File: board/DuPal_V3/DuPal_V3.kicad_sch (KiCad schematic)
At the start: 63 parts, among them J1 ZIF Socket, K1 G6K-2, Q1 2N3904, U1 Pico, U10 74HCT166, U11 74HCT166, U12 74HCT166, U13 SN74LV1T125DBV, U2 74HCT595, U3 74HCT595, U4 74HCT595, U5 74HCT595, U6 74HCT595, U7 74HCT02, U8 74HCT166, U9 74HCT166

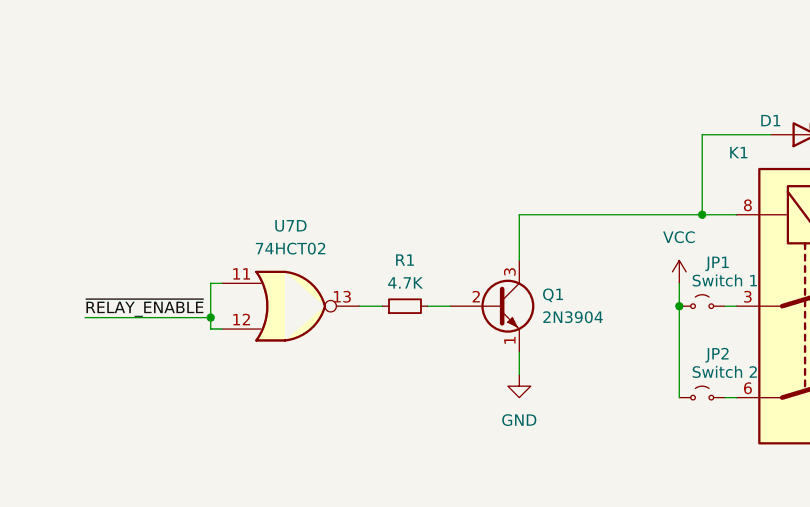
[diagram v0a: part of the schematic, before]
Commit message: Change resistor value
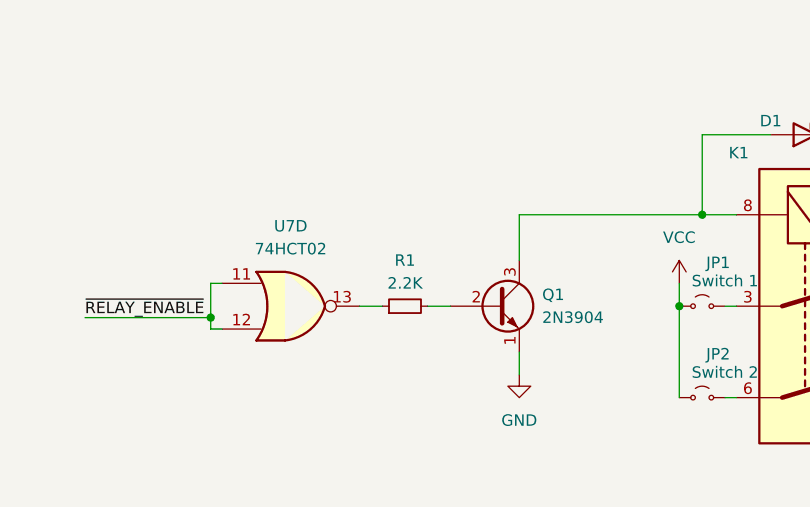
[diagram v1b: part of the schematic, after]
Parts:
- R1: value 4.7K -> 2.2K
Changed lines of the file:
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@@
 			)
 		)
-		(property "Value" "4.7K"
+		(property "Value" "2.2K"
 			(at 91.44 261.62 90)
 			(effects

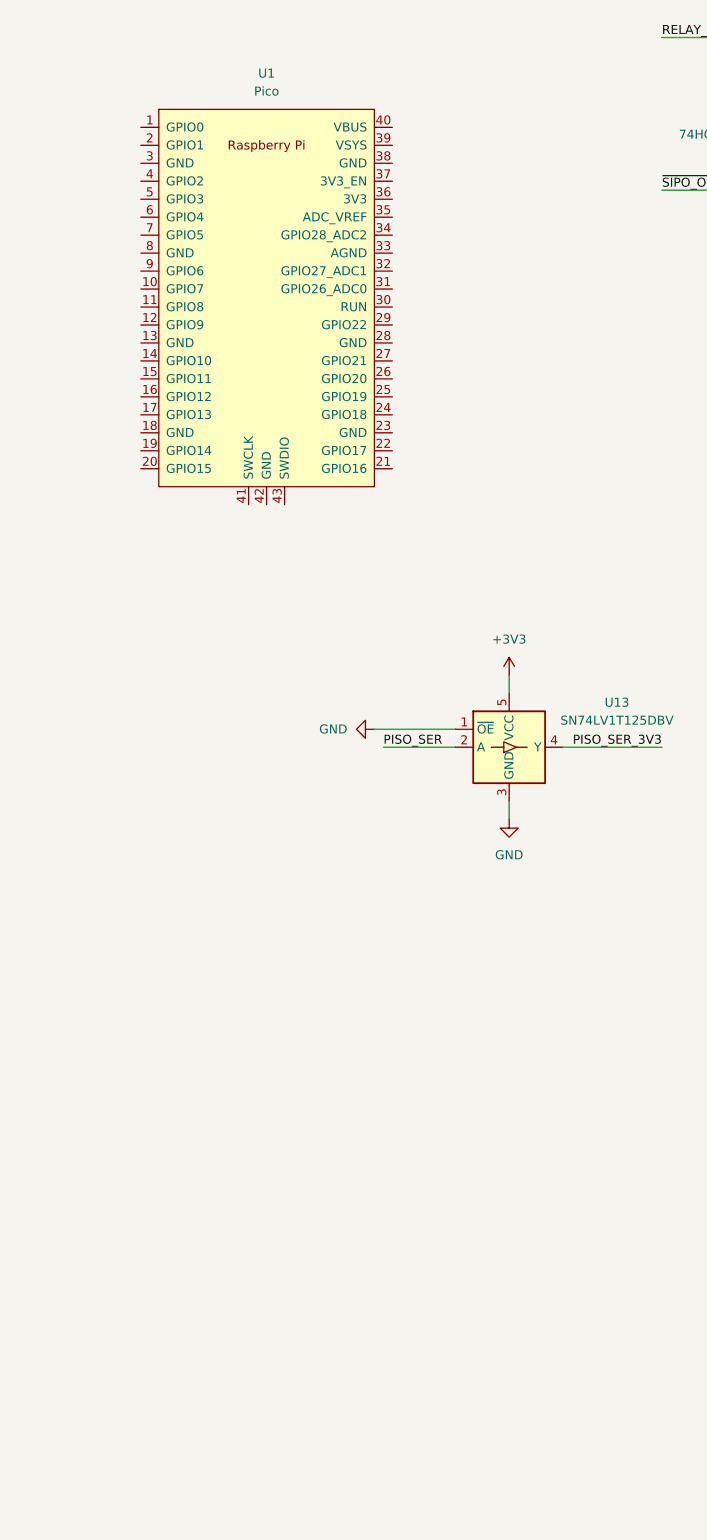
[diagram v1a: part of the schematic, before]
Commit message: Add connections to pico
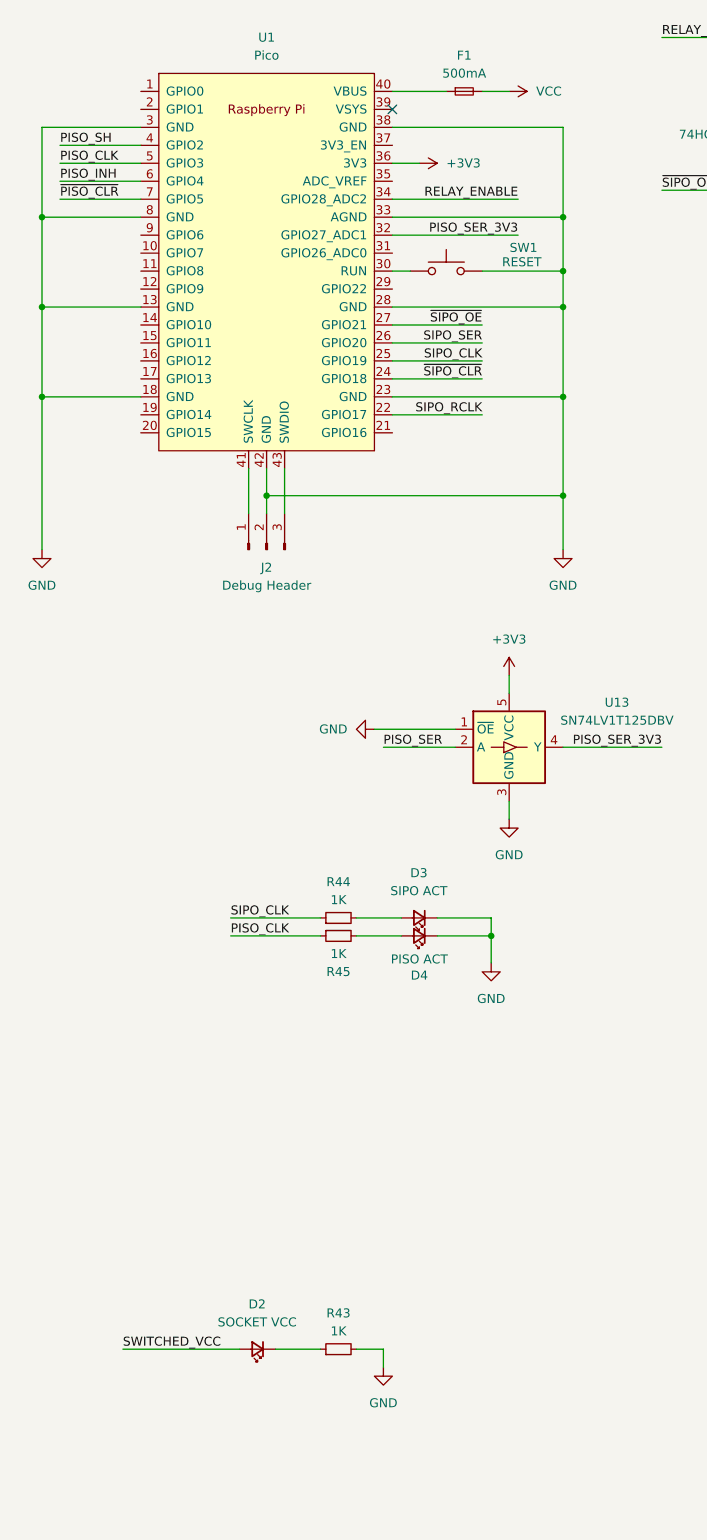
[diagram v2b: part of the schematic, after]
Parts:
- added D2: SOCKET VCC, symbol Device:LED_Small
- added D3: SIPO ACT, symbol Device:LED_Small
- added D4: PISO ACT, symbol Device:LED_Small
- added F1: 500mA, symbol Device:Fuse_Small
- added J2: Debug Header, symbol Connector:Conn_01x03_Pin
- added R43, R44, R45: 1K, symbol Device:R_Small
- added SW1: RESET, symbol Switch:SW_Push
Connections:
- net +3V3: now also U1.36 (3V3)
- net GND: now also U1.13 (GND), U1.18 (GND), U1.23 (GND), U1.28 (GND), U1.3 (GND), U1.33 (AGND), U1.38 (GND), U1.42 (GND), U1.8 (GND), D3.1 (K), D4.1 (K), J2.2 (Pin_2), R43.2, SW1.2
- net PISO_CLK: now also U1.5 (GPIO3), R45.1
- net PISO_INH: now also U1.6 (GPIO4)
- net PISO_SER_3V3: now also U1.32 (GPIO27_ADC1)
- net PISO_SH: now also U1.4 (GPIO2)
- net RELAY_ENABLE: now also U1.34 (GPIO28_ADC2)
- net SIPO_CLK: now also U1.25 (GPIO19), R44.1
- net SIPO_RCLK: now also U1.22 (GPIO17)
- net SIPO_SER: now also U1.26 (GPIO20)
- net SWITCHED_VCC: now also D2.2 (A)
- net VCC: now also F1.2
- net ~{PISO_CLR}: now also U1.7 (GPIO5)
- net ~{SIPO_CLR}: now also U1.24 (GPIO18)
- net ~{SIPO_OE}: now also U1.27 (GPIO21)
- net at U1.30 (RUN): now also SW1.1
- net at U1.40 (VBUS): now also F1.1
- net at U1.41 (SWCLK): now also J2.1 (Pin_1)
- net at U1.43 (SWDIO): now also J2.3 (Pin_3)
- new net: D4.2 (A), R45.2
- new net: D3.2 (A), R44.2
- new net: D2.1 (K), R43.1
- no-connect marks 3 -> 4
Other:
- moved on the sheet: U1

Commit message: Add pulldown resistors for socket
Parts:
- added R46, R47, R48, R49, R50, R51, R52, R53, R54, R55, R56, R57, R58, R59, R60, R61, R62, R63, R64, R65, R66, R67, R68, R69, R70, R71, R72, R73, R74, R75, R76, R77, R78, R79, R80, R81, R82, R83, R84, R85: 100K, symbol Device:R_Small
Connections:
- net GND: now also R46.2, R47.2, R48.2, R49.2, R50.2, R51.2, R52.2, R53.2, R54.2, R55.2, R56.2, R57.2, R58.2, R59.2, R60.2, R61.2, R62.2, R63.2, R64.2, R65.2, R66.2, R67.2, R68.2, R69.2, R70.2, R71.2, R72.2, R73.2, R74.2, R75.2, R76.2, R77.2, R78.2, R79.2, R80.2, R81.2, R82.2, R83.2, R84.2, R85.2
- net SWITCHED_VCC: now also U7.2, U7.3
- net ZIF_1: now also R46.1
- net ZIF_10: now also R55.1
- net ZIF_11: now also R56.1
- net ZIF_12: now also R57.1
- net ZIF_13: now also R58.1
- net ZIF_14: now also R59.1
- net ZIF_15: now also R60.1
- net ZIF_16: now also R61.1
- net ZIF_17: now also R62.1
- net ZIF_18: now also R63.1
- net ZIF_19: now also R64.1
- net ZIF_2: now also R47.1
- net ZIF_20: now also R65.1
- net ZIF_22: now also R66.1
- net ZIF_23: now also R67.1
- net ZIF_24: now also R68.1
- net ZIF_25: now also R69.1
- net ZIF_26: now also R70.1
- net ZIF_27: now also R71.1
- net ZIF_28: now also R72.1
- net ZIF_29: now also R73.1
- net ZIF_3: now also R48.1
- net ZIF_30: now also R74.1
- net ZIF_31: now also R75.1
- net ZIF_32: now also R76.1
- net ZIF_33: now also R77.1
- net ZIF_34: now also R78.1
- net ZIF_35: now also R79.1
- net ZIF_36: now also R80.1
- net ZIF_37: now also R81.1
- net ZIF_38: now also R82.1
- net ZIF_39: now also R83.1
- net ZIF_4: now also R49.1
- net ZIF_40: now also R84.1
- net ZIF_41: now also R85.1
- net ZIF_5: now also R50.1
- net ZIF_6: now also R51.1
- net ZIF_7: now also R52.1
- net ZIF_8: now also R53.1
- net ZIF_9: now also R54.1
- net ~{RELAY_ENABLE}: now also U1.34 (GPIO28_ADC2); no longer U7.1, U7.5
- removed net RELAY_ENABLE: U1.34 (GPIO28_ADC2), U7.2, U7.3
- new net: U7.1, U7.5
- no-connect marks 4 -> 20
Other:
- moved on the sheet: C1, C2, R42

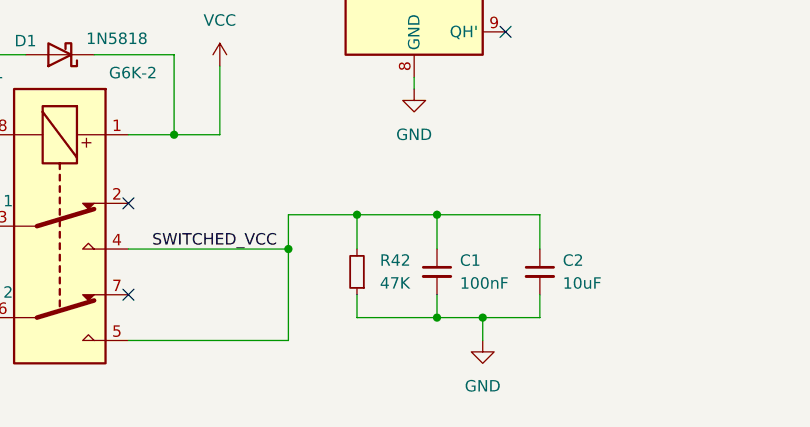
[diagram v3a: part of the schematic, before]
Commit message: Change pulldown res on switched VCC value
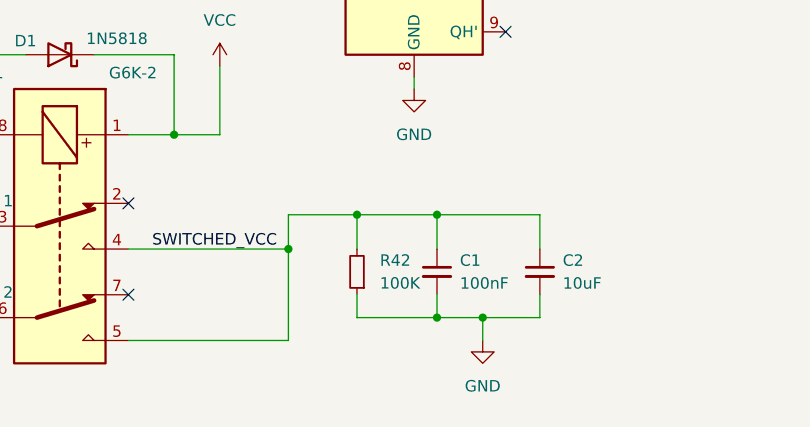
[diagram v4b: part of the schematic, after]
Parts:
- R42: value 47K -> 100K
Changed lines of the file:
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@@
 			)
 		)
-		(property "Value" "47K"
+		(property "Value" "100K"
 			(at 171.45 270.5099 0)
 			(effects

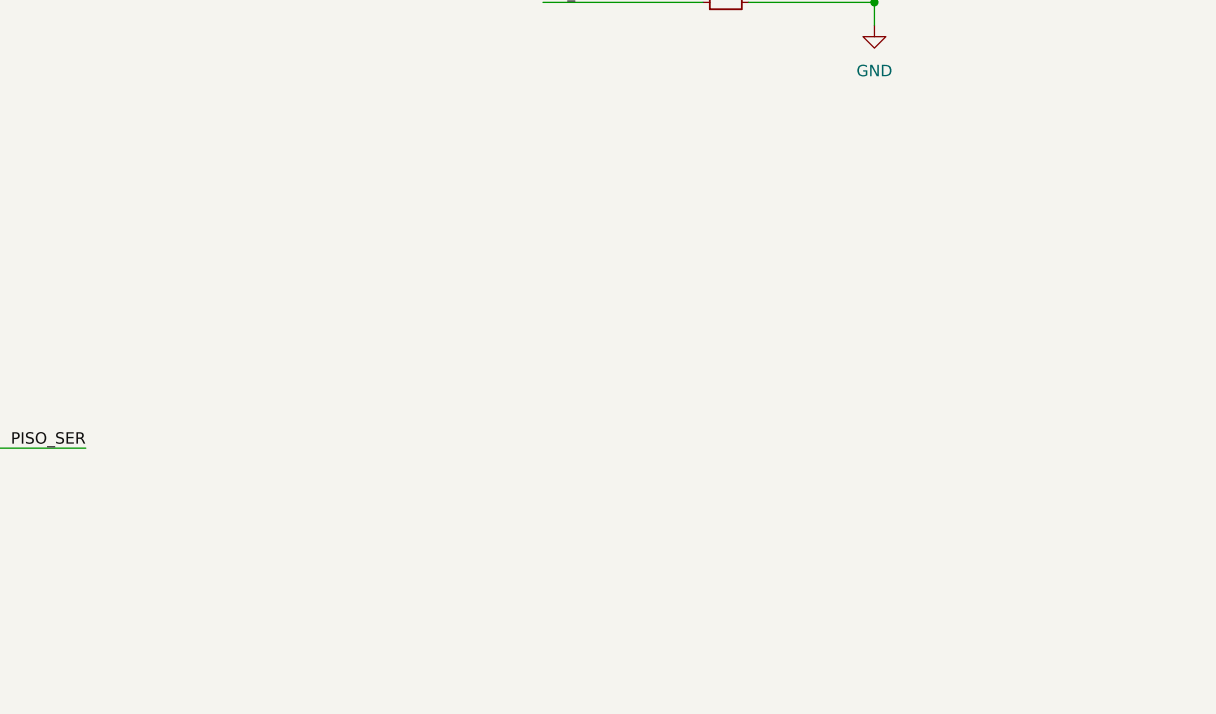
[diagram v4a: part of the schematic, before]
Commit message: Assigned footprints
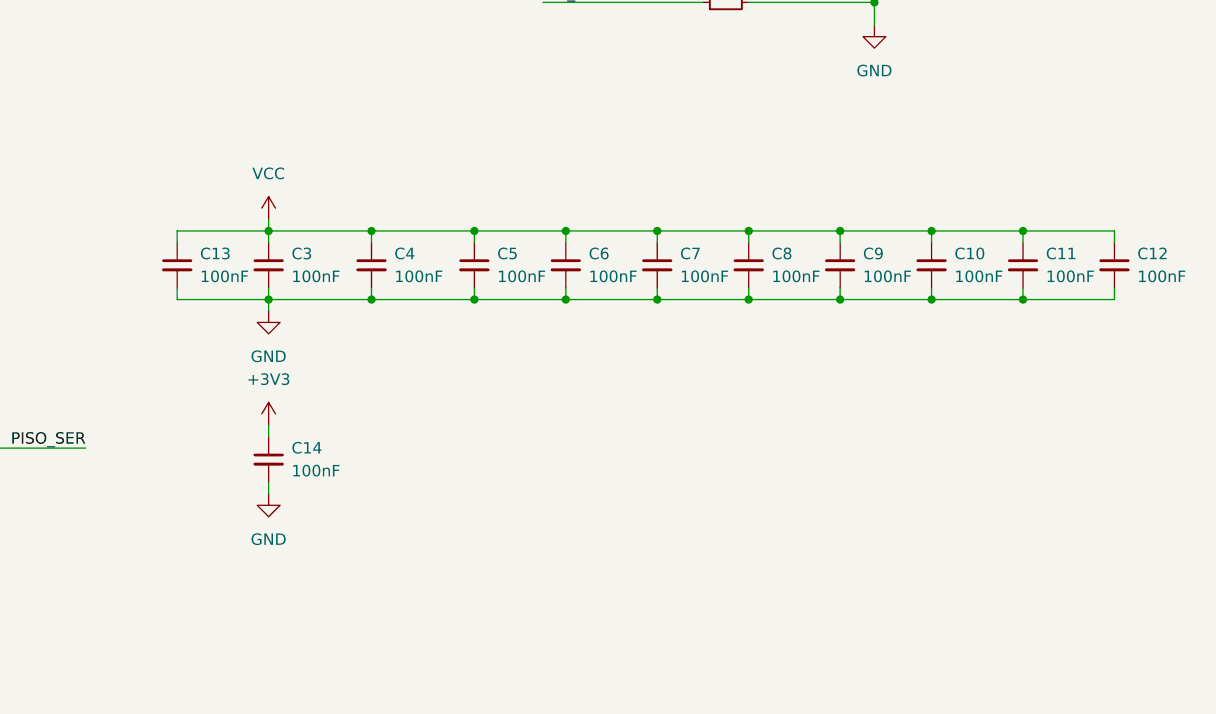
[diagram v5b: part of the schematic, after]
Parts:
- added C10, C11, C12, C13, C14, C3, C4, C5, C6, C7, C8, C9: 100nF, Capacitor_SMD:C_1206_3216Metric_Pad1.33x1.80mm_HandSolder, symbol Device:C_Small
- C1, C2: footprint (none) -> Capacitor_SMD:C_1206_3216Metric_Pad1.33x1.80mm_HandSolder
- D2, D3, D4: footprint (none) -> LED_SMD:LED_1206_3216Metric_Pad1.42x1.75mm_HandSolder
- F1: footprint (none) -> Fuse:Fuse_1206_3216Metric_Pad1.42x1.75mm_HandSolder
- J2: footprint (none) -> Connector_PinHeader_2.54mm:PinHeader_1x03_P2.54mm_Vertical
- JP1, JP2: footprint (none) -> Jumper:SolderJumper-2_P1.3mm_Open_RoundedPad1.0x1.5mm
- K1: footprint (none) -> Relay_THT:Relay_DPDT_Omron_G6K-2P-Y
- R1, R10, R11, R12, R13, R14, R15, R16, R17, R18, R19, R2, R20, R21, R22, R23, R24, R25, R26, R27, R28, R29, R3, R30, R31, R32, R33, R34, R35, R36, R37, R38, R39, R4, R40, R41, R42, R43, R44, R45, R46, R47, R48, R49, R5, R50, R51, R52, R53, R54, R55, R56, R57, R58, R59, R6, R60, R61, R62, R63, R64, R65, R66, R67, R68, R69, R7, R70, R71, R72, R73, R74, R75, R76, R77, R78, R79, R8, R80, R81, R82, R83, R84, R85, R9: footprint (none) -> Resistor_SMD:R_1206_3216Metric_Pad1.30x1.75mm_HandSolder
- SW1: footprint (none) -> Button_Switch_THT:SW_PUSH_6mm
- U10, U11, U12, U2, U3, U4, U5, U6, U8, U9: footprint (none) -> Package_SO:SOIC-16_3.9x9.9mm_P1.27mm
- U7: footprint (none) -> Package_SO:SOIC-14_3.9x8.7mm_P1.27mm
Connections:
- net +3V3: now also C14.1
- net GND: now also C10.2, C11.2, C12.2, C13.2, C14.2, C3.2, C4.2, C5.2, C6.2, C7.2, C8.2, C9.2
- net VCC: now also C10.1, C11.1, C12.1, C13.1, C3.1, C4.1, C5.1, C6.1, C7.1, C8.1, C9.1

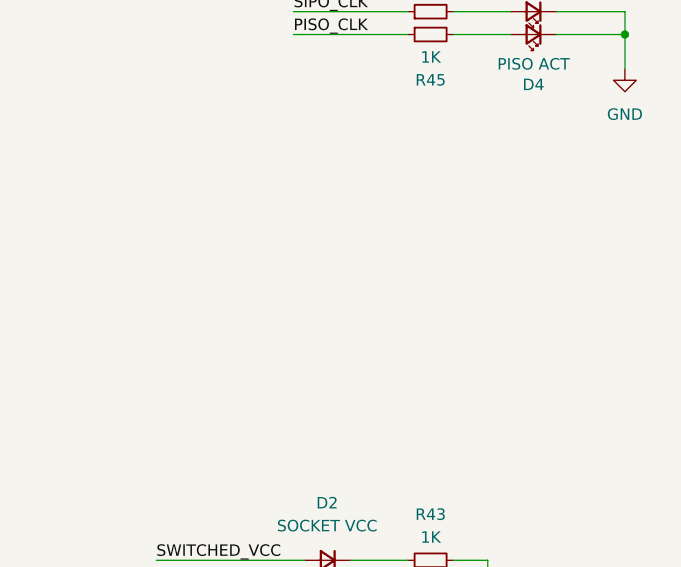
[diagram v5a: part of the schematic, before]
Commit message: Added mounting holes
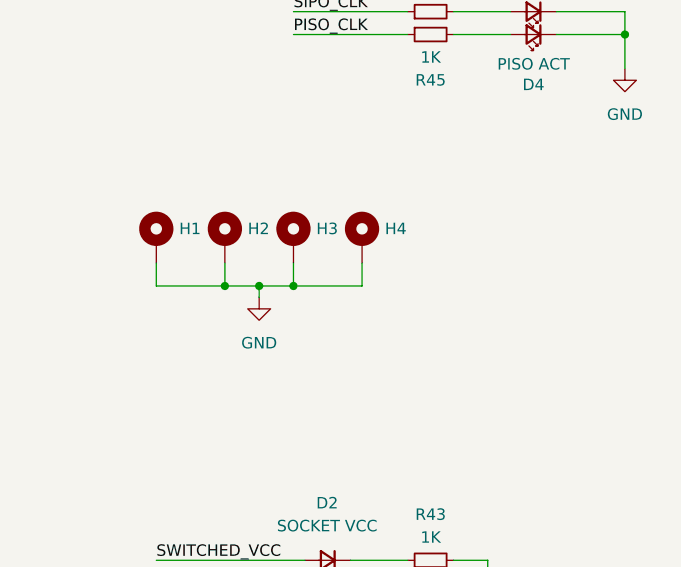
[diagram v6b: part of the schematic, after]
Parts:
- added H1, H2, H3, H4: MountingHole_Pad, MountingHole:MountingHole_3.2mm_M3_DIN965_Pad, symbol Mechanical:MountingHole_Pad
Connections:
- net GND: now also H1.1, H2.1, H3.1, H4.1

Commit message: Cleanup
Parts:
- R43: value 1K -> 1.2K
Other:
- moved on the sheet: C1, C2, D1, D2, JP1, JP2, K1, Q1, R1, R42, R43, U7D

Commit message: Update board
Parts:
- R46, R47, R48, R49, R50, R51, R52, R53, R54, R55, R56, R57, R58, R59, R60, R61, R62, R63, R64, R65, R66, R67, R68, R69, R70, R71, R72, R73, R74, R75, R76, R77, R78, R79, R80, R81, R82, R83, R84, R85: value 100K -> 470K
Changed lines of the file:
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@@
 			)
 		)
-		(property "Value" "100K"
+		(property "Value" "470K"
 			(at 353.822 179.324 90)
 			(effects
@@
 			)
 		)
-		(property "Value" "100K"
+		(property "Value" "470K"
 			(at 353.822 151.384 90)
 			(effects
@@
 			)
 		)
-		(property "Value" "100K"
+		(property "Value" "470K"
 			(at 353.822 176.784 90)
 			(effects
@@
 			)
 		)
-		(property "Value" "100K"
+		(property "Value" "470K"
 			(at 353.822 184.404 90)
 			(effects
@@
 			)
 		)
-		(property "Value" "100K"
+		(property "Value" "470K"
 			(at 353.822 115.824 90)
 			(effects
@@
 			)
 		)
-		(property "Value" "100K"
+		(property "Value" "470K"
 			(at 353.822 105.664 90)
 			(effects
@@
 			)
 		)
-		(property "Value" "100K"
+		(property "Value" "470K"
 			(at 353.822 128.524 90)
 			(effects
@@
 			)
 		)
-		(property "Value" "100K"
+		(property "Value" "470K"
 			(at 353.822 169.164 90)
 			(effects
@@
 			)
 		)
-		(property "Value" "100K"
+		(property "Value" "470K"
 			(at 353.822 103.124 90)
 			(effects
@@
 			)
 		)
-		(property "Value" "100K"
+		(property "Value" "470K"
 			(at 353.822 136.144 90)
 			(effects
@@
 			)
 		)
-		(property "Value" "100K"
+		(property "Value" "470K"
 			(at 353.822 189.484 90)
 			(effects
@@
 			)
 		)
-		(property "Value" "100K"
+		(property "Value" "470K"
 			(at 353.822 148.844 90)
 			(effects
@@
 			)
 		)
-		(property "Value" "100K"
+		(property "Value" "470K"
 			(at 353.822 141.224 90)
 			(effects
@@
 			)
 		)
-		(property "Value" "100K"
+		(property "Value" "470K"
 			(at 353.822 159.004 90)
 			(effects
@@
 			)
 		)
-		(property "Value" "100K"
+		(property "Value" "470K"
 			(at 353.822 161.544 90)
 			(effects
@@
 			)
 		)
-		(property "Value" "100K"
+		(property "Value" "470K"
 			(at 353.822 123.444 90)
 			(effects
@@
 			)
 		)
-		(property "Value" "100K"
+		(property "Value" "470K"
 			(at 353.822 110.744 90)
 			(effects
@@
 			)
 		)
-		(property "Value" "100K"
+		(property "Value" "470K"
 			(at 353.822 98.044 90)
 			(effects
@@
 			)
 		)
-		(property "Value" "100K"
+		(property "Value" "470K"
 			(at 353.822 118.364 90)
 			(effects
@@
 			)
 		)
-		(property "Value" "100K"
+		(property "Value" "470K"
 			(at 353.822 133.604 90)
 			(effects
@@
 			)
 		)
-		(property "Value" "100K"
+		(property "Value" "470K"
 			(at 353.822 131.064 90)
 			(effects
@@
 			)
 		)
-		(property "Value" "100K"
+		(property "Value" "470K"
 			(at 353.822 143.764 90)
 			(effects
@@
 			)
 		)
-		(property "Value" "100K"
+		(property "Value" "470K"
 			(at 353.822 113.284 90)
 			(effects
@@
 			)
 		)
-		(property "Value" "100K"
+		(property "Value" "470K"
 			(at 353.822 153.924 90)
 			(effects
@@
 			)
 		)
-		(property "Value" "100K"
+		(property "Value" "470K"
 			(at 353.822 181.864 90)
 			(effects
@@
 			)
 		)
-		(property "Value" "100K"
+		(property "Value" "470K"
 			(at 353.822 171.704 90)
 			(effects
@@
 			)
 		)
-		(property "Value" "100K"
+		(property "Value" "470K"
 			(at 353.822 120.904 90)
 			(effects
@@
 			)
 		)
-		(property "Value" "100K"
+		(property "Value" "470K"
 			(at 353.822 146.304 90)
 			(effects
@@
 			)
 		)
-		(property "Value" "100K"
+		(property "Value" "470K"
 			(at 353.822 125.984 90)
 			(effects
@@
 			)
 		)
-		(property "Value" "100K"
+		(property "Value" "470K"
 			(at 353.822 174.244 90)
 			(effects
@@
 			)
 		)
-		(property "Value" "100K"
+		(property "Value" "470K"
 			(at 353.822 164.084 90)
 			(effects
@@
 			)
 		)
-		(property "Value" "100K"
+		(property "Value" "470K"
 			(at 353.822 100.584 90)
 			(effects
@@
 			)
 		)
-		(property "Value" "100K"
+		(property "Value" "470K"
 			(at 353.822 90.424 90)
 			(effects
@@
 			)
 		)
-		(property "Value" "100K"
+		(property "Value" "470K"
 			(at 353.822 95.504 90)
 			(effects
@@
 			)
 		)
-		(property "Value" "100K"
+		(property "Value" "470K"
 			(at 353.822 138.684 90)
 			(effects
@@
 			)
 		)
-		(property "Value" "100K"
+		(property "Value" "470K"
 			(at 353.822 156.464 90)
 			(effects
@@
 			)
 		)
-		(property "Value" "100K"
+		(property "Value" "470K"
 			(at 353.822 92.964 90)
 			(effects
@@
 			)
 		)
-		(property "Value" "100K"
+		(property "Value" "470K"
 			(at 353.822 166.624 90)
 			(effects
@@
 			)
 		)
-		(property "Value" "100K"
+		(property "Value" "470K"
 			(at 353.822 186.944 90)
 			(effects
@@
 			)
 		)
-		(property "Value" "100K"
+		(property "Value" "470K"
 			(at 353.822 108.204 90)
 			(effects
